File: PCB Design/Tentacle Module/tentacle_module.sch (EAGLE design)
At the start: 58 parts, among them IC1 5.0V, IC3 3.3V, T1 NTD5867NL, T2 NTD5867NL, T3 NTD5867NL, T4 NTD5867NL, U1 OKR-T/10-W12, X3 RJ45-8X, X4 RJ45-8X

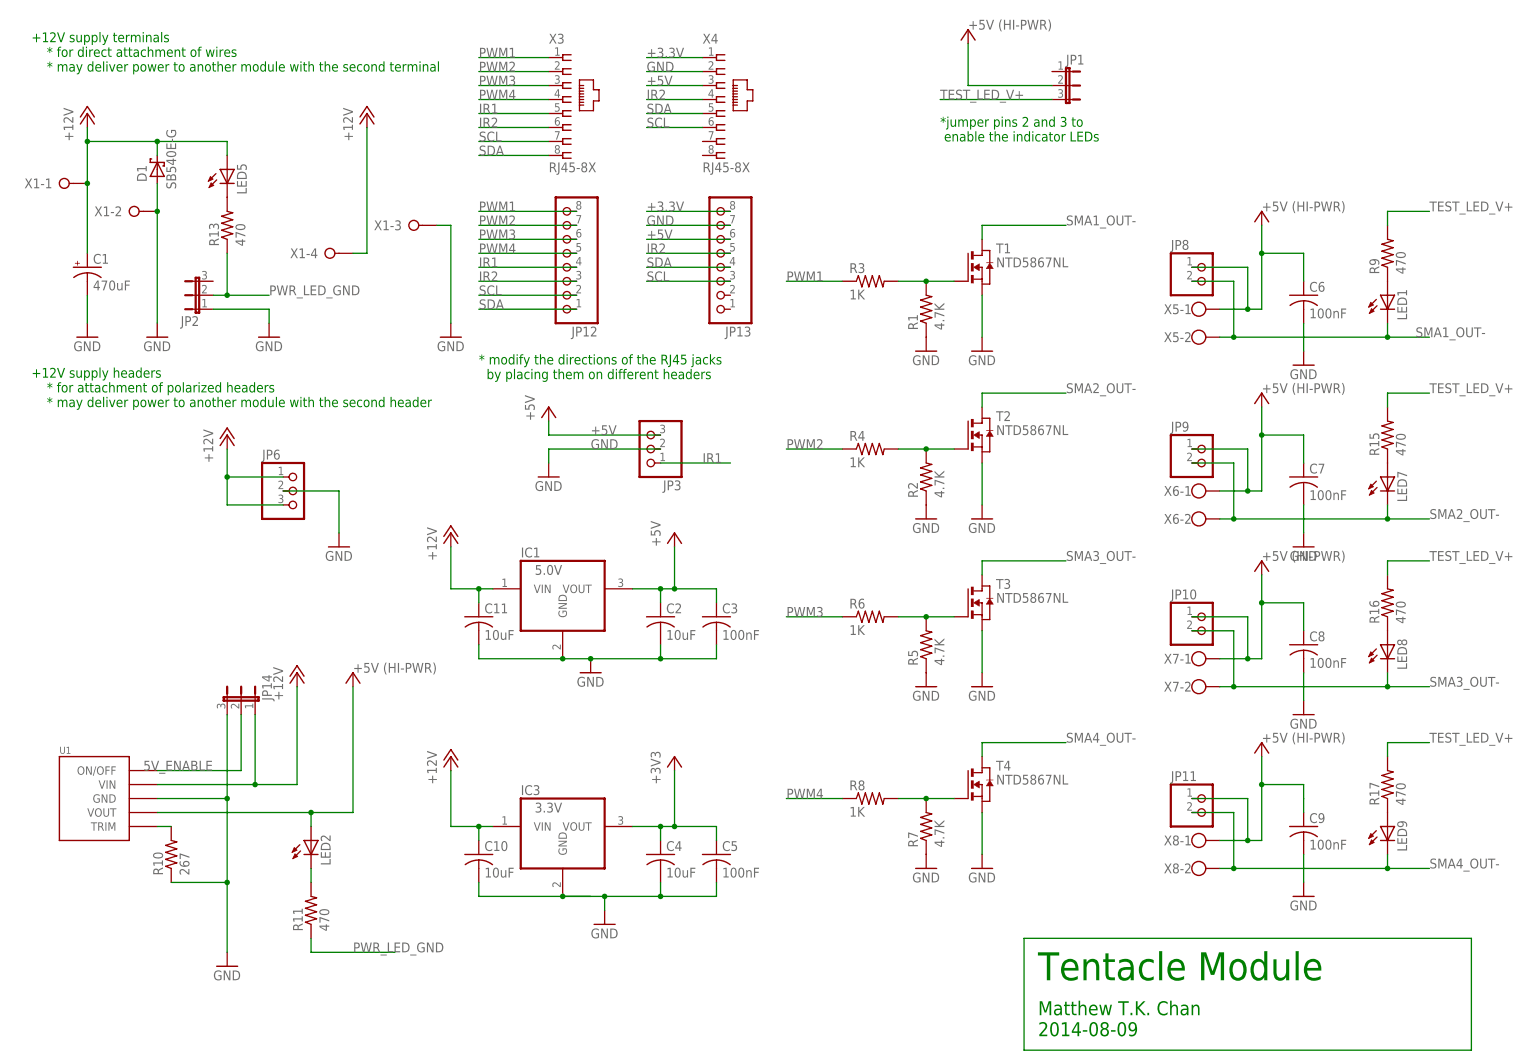
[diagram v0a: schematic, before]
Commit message: removed the unnecesssary by-pass cap by the v-reg
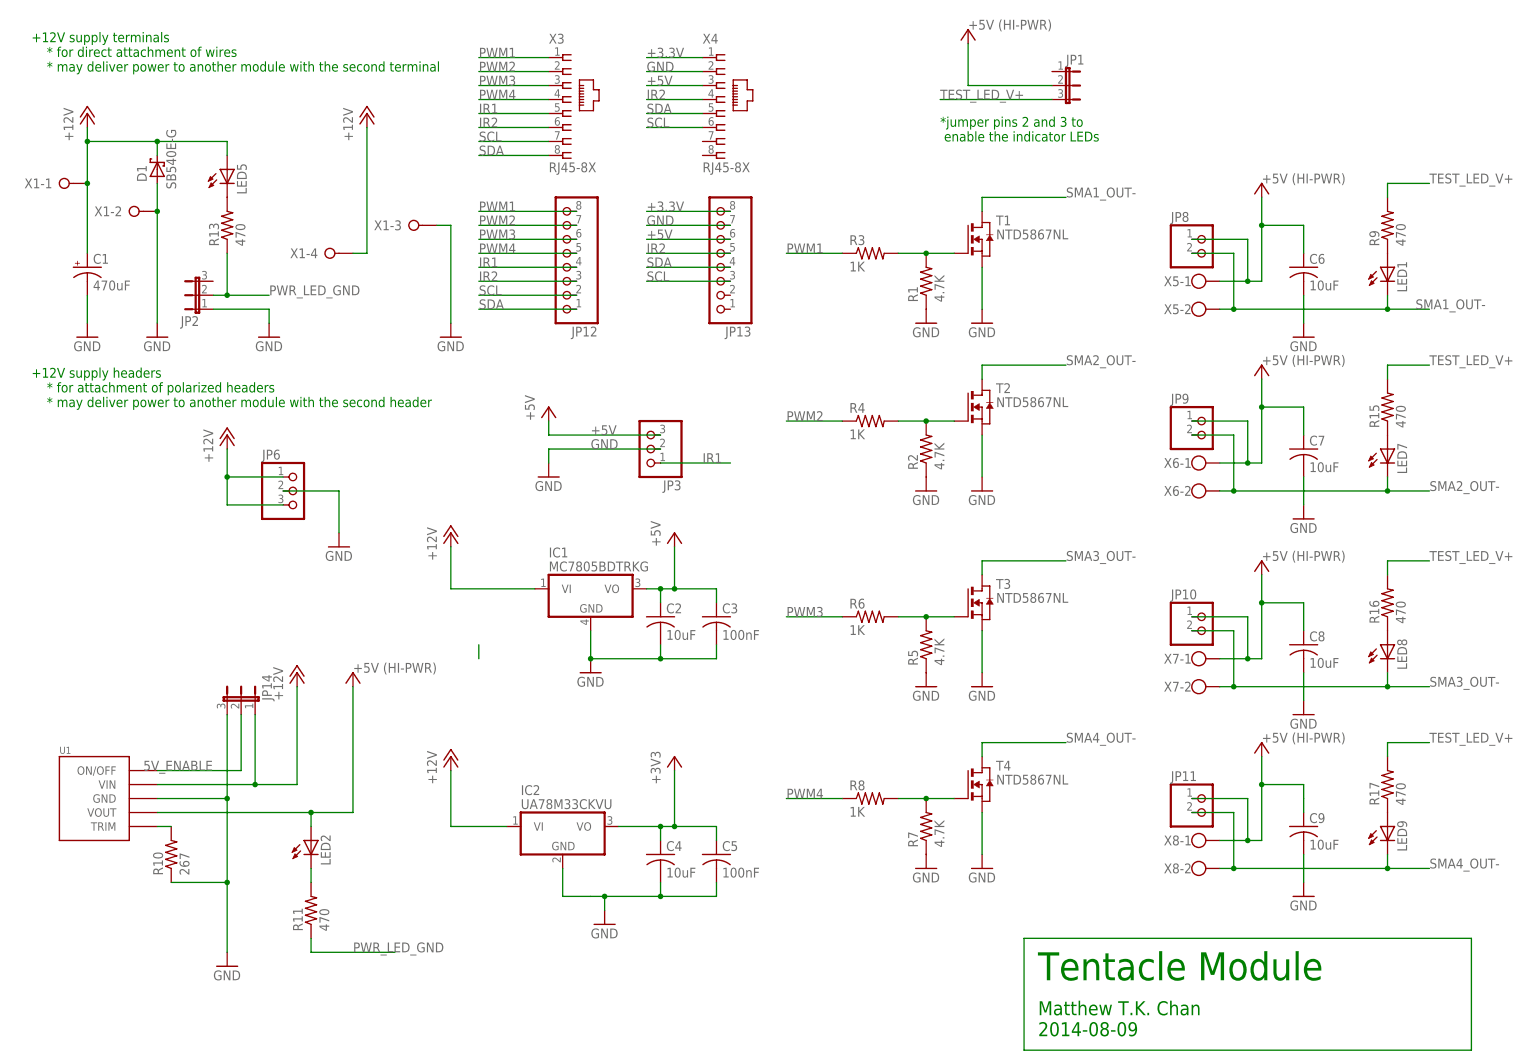
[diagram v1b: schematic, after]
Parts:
- removed C10, C11: 10uF, rcl:C-USC0603
- removed IC3: 3.3V, CBLA_Test_bed_Library:REG11173.3VDT
- added IC2: UA78M33CKVU, CBLA_Test_bed_Library:UA78M33CKVU
- C6, C7, C8, C9: value 100nF -> 10uF
- IC1: value 5.0V -> MC7805BDTRKG; device CBLA_Test_bed_Library:REG11175.0VDT -> CBLA_Test_bed_Library:MC7805BDTRKG
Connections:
- net +12V: now also IC1.VI, IC2.VI; no longer C10.1, C11.1, IC1.VIN, IC3.VIN
- net +3.3V: now also IC2.VO; no longer IC3.VOUT
- net +5V: now also IC1.VO; no longer IC1.VOUT
- net GND: now also IC2.GND; no longer C10.2, C11.2, IC3.GND
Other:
- note removed: "* modify the directions of the RJ45 jacks by placing them on different headers"
- moved on the sheet: C6, C7, IC1, JP8, JP9, LED1, LED7, R1, R15, R2, R3, R4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

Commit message: Edited the silkscreen for Tentacle board
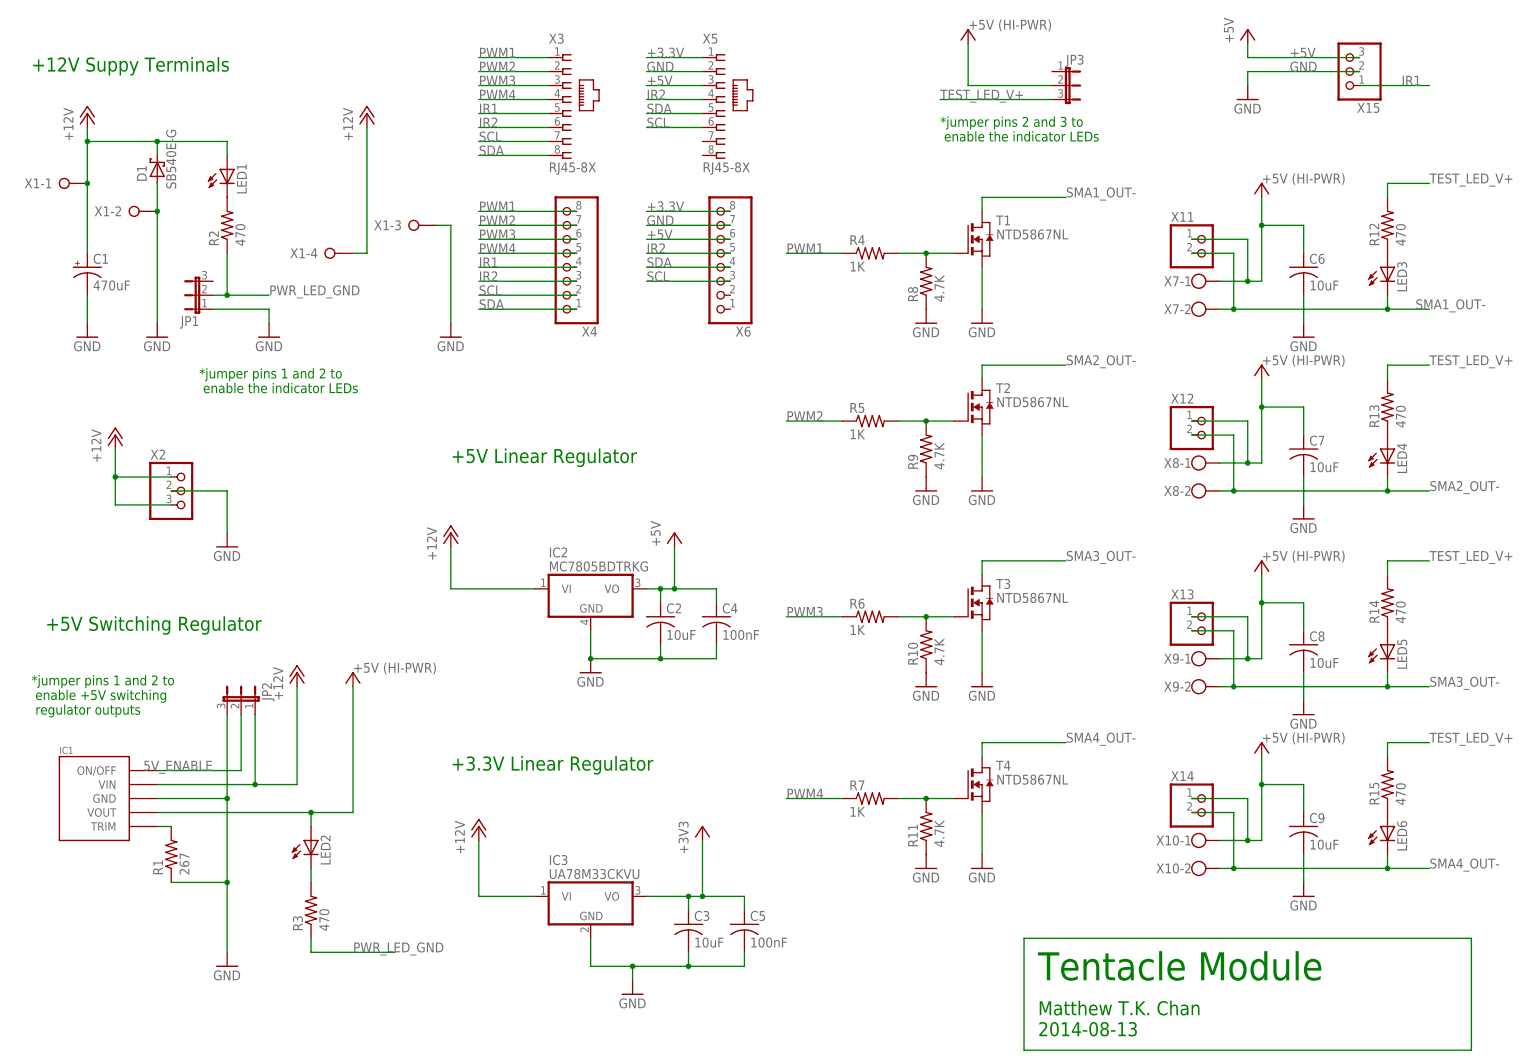
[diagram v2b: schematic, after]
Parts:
- removed JP12, JP13: (no value), CBLA_Test_bed_Library:PINHD-1X8
- removed JP14: (no value), jumper:JP2E
- removed JP6: (no value), CBLA_Test_bed_Library:PINHD-1X3/90
- removed LED8: (no value), led:LEDSML1206
- removed R17: 470, CBLA_Test_bed_Library:R-US_R0603
- removed U1: OKR-T/10-W12, CBLA_Test_bed_Library:OKR-T/10-W12
- added IC3: UA78M33CKVU, CBLA_Test_bed_Library:UA78M33CKVU
- added LED3: (no value), led:LEDSML1206
- added R12: 470, CBLA_Test_bed_Library:R-US_R0603
- added X10, X9: (no value), con-wago-500:W237-102
- added X15, X2: (no value), CBLA_Test_bed_Library:PINHD-1X3/90
- C3: value 100nF -> 10uF
- C4: value 10uF -> 100nF
- IC1: value MC7805BDTRKG -> OKR-T/10-W12; device CBLA_Test_bed_Library:MC7805BDTRKG -> CBLA_Test_bed_Library:OKR-T/10-W12
- IC2: value UA78M33CKVU -> MC7805BDTRKG; device CBLA_Test_bed_Library:UA78M33CKVU -> CBLA_Test_bed_Library:MC7805BDTRKG
- JP3: device CBLA_Test_bed_Library:PINHD-1X3/90 -> jumper:JP2E
- R1: value 4.7K -> 267
- R10: value 267 -> 4.7K
- R11, R9: value 470 -> 4.7K
- R2: value 4.7K -> 470
- R3: value 1K -> 470
- R5, R7: value 4.7K -> 1K
- R8: value 1K -> 4.7K
- X4: value RJ45-8X -> (none); device CBLA_Test_bed_Library:RJ45-8X -> CBLA_Test_bed_Library:PINHD-1X8
- X5: value (none) -> RJ45-8X; device con-wago-500:W237-102 -> CBLA_Test_bed_Library:RJ45-8X
- X6: device con-wago-500:W237-102 -> CBLA_Test_bed_Library:PINHD-1X8
- renumbered JP10 to X13, JP11 to X14, JP8 to X11, JP9 to X12, LED7 to LED4, LED9 to LED6, R16 to R14
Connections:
- net +12V: now also IC1.VIN, IC3.VI, JP2.1, LED1.A, X2.1, X2.3; no longer IC1.VI, JP14.1, JP6.1, JP6.3, LED5.A, U1.VIN
- net +3.3V: now also C3.1, IC3.VO, X5.1, X6.8; no longer C4.1, IC2.VO, JP13.8, X4.1
- net +5V: now also C4.1, IC2.VO, X15.3, X5.3, X6.6; no longer C3.1, IC1.VO, JP13.6, JP3.3, X4.3
- net +5V_HI-PWR: now also IC1.VOUT, JP3.2, X10-1.KL, X9-1.KL; no longer JP1.2, U1.VOUT, X5-1.KL, X6-1.KL
- net 5V_ENABLE: now also IC1.ON/OFF, JP2.2; no longer JP14.2, U1.ON/OFF
- net GND: now also IC3.GND, JP1.1, JP2.3, R11.1, R8.1, R9.1, X15.2, X2.2, X5.2, X6.7; no longer JP13.7, JP14.3, JP2.1, JP3.2, JP6.2, R2.1, R5.1, R7.1, U1.GND, X4.2
- net IR1: now also X15.1, X4.4; no longer JP12.4, JP3.1
- net IR2: now also X4.3, X5.4, X6.5; no longer JP12.3, JP13.5, X4.4
- net N$1: now also R5.2, R9.2; no longer R2.2, R4.2
- net N$10: now also LED1.C, R2.2; no longer LED5.C, R13.2
- net N$12: now also R13.1; no longer R15.1
- net N$13: now also LED5.A; no longer LED8.A
- net N$14: now also R15.1; no longer R17.1
- net N$2: now also R10.2; no longer R5.2
- net N$3: now also R11.2; no longer R8.2
- net N$4: now also R4.2, R8.2; no longer R1.2, R3.2
- net N$5: now also LED3.A, R12.1; no longer LED1.A, R9.1
- net N$6: now also IC1.TRIM, R1.2; no longer R10.2, U1.TRIM
- net N$7: now also R3.2; no longer R11.2
- net PWM1: now also R4.1, X4.8; no longer JP12.8, R3.1
- net PWM2: now also R5.1, X4.7; no longer JP12.7, R4.1
- net PWM3: now also X4.6; no longer JP12.6
- net PWM4: now also R7.1, X4.5; no longer JP12.5, R8.1
- net PWR_LED_GND: now also JP1.2, R2.1, R3.1; no longer JP2.2, R11.1, R13.1
- net SCL: now also X4.2, X5.6, X6.3; no longer JP12.2, JP13.3, X4.6
- net SDA: now also X4.1, X5.5, X6.4; no longer JP12.1, JP13.4, X4.5
- net SMA1_OUT-: now also LED3.C, X7-2.KL; no longer LED1.C, X5-2.KL
- net SMA2_OUT-: now also X8-2.KL; no longer X6-2.KL
- net SMA3_OUT-: now also LED5.C, X9-2.KL; no longer LED8.C, X7-2.KL
- net SMA4_OUT-: now also X10-2.KL; no longer X8-2.KL
- net TEST_LED_V+: now also JP3.3, R12.2, R13.2; no longer JP1.3, R17.2, R9.2
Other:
- note added: "*jumper pins 1 and 2 to enable +5V switching regulator outputs"
- note added: "*jumper pins 1 and 2 to enable the indicator LEDs"
- note added: "+12V Suppy Terminals"
- note added: "+3.3V Linear Regulator"
- note added: "+5V Linear Regulator"
- note added: "+5V Switching Regulator"
- note added: "Matthew T.K. Chan 2014-08-13"
- note removed: "+12V supply headers * for attachment of polarized headers * may deliver power to another module with the second header"
- note removed: "+12V supply terminals * for direct attachment of wires * may deliver power to another module with the second terminal"
- note removed: "Matthew T.K. Chan 2014-08-09"
- moved on the sheet: C3, C4, C5, IC2, JP1, JP2, LED1, LED5, R1, R10, R11, R13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

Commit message: Swapped the SDA and SCL pins on the Tentacle tip connector
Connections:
- net SCL: now also X5.5, X6.4; no longer X5.6, X6.3
- net SDA: now also X5.6, X6.3; no longer X5.5, X6.4
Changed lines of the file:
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@@
-</segment>
-<segment>
-<pinref part="X5" gate="G$1" pin="6"/>
-<wire x1="137.16" y1="175.26" x2="127" y2="175.26" width="0.1524" layer="91"/>
-<label x="127" y="175.26" size="1.778" layer="95"/>
 </segment>
 <segment>
@@
 </segment>
 <segment>
-<wire x1="142.24" y1="147.32" x2="127" y2="147.32" width="0.1524" layer="91"/>
-<label x="127" y="147.32" size="1.778" layer="95"/>
-<pinref part="X6" gate="A" pin="3"/>
+<pinref part="X5" gate="G$1" pin="5"/>
+<wire x1="137.16" y1="177.8" x2="127" y2="177.8" width="0.1524" layer="91"/>
+<label x="127" y="177.8" size="1.778" layer="95"/>
+</segment>
+<segment>
+<wire x1="142.24" y1="149.86" x2="127" y2="149.86" width="0.1524" layer="91"/>
+<label x="127" y="149.86" size="1.778" layer="95"/>
+<pinref part="X6" gate="A" pin="4"/>
 </segment>
 </net>
@@
 </segment>
 <segment>
-<pinref part="X5" gate="G$1" pin="5"/>
-<wire x1="137.16" y1="177.8" x2="127" y2="177.8" width="0.1524" layer="91"/>
-<label x="127" y="177.8" size="1.778" layer="95"/>
-</segment>
-<segment>
 <wire x1="114.3" y1="142.24" x2="96.52" y2="142.24" width="0.1524" layer="91"/>
 <label x="96.52" y="142.24" size="1.778" layer="95"/>
@@
 </segment>
 <segment>
-<wire x1="142.24" y1="149.86" x2="127" y2="149.86" width="0.1524" layer="91"/>
-<label x="127" y="149.86" size="1.778" layer="95"/>
-<pinref part="X6" gate="A" pin="4"/>
+<pinref part="X5" gate="G$1" pin="6"/>
+<wire x1="137.16" y1="175.26" x2="127" y2="175.26" width="0.1524" layer="91"/>
+<label x="127" y="175.26" size="1.778" layer="95"/>
+</segment>
+<segment>
+<wire x1="142.24" y1="147.32" x2="127" y2="147.32" width="0.1524" layer="91"/>
+<label x="127" y="147.32" size="1.778" layer="95"/>
+<pinref part="X6" gate="A" pin="3"/>
 </segment>
 </net>
